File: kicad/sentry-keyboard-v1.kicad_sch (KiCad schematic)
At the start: 272 parts, among them J1 USB_C_Receptacle_USB2.0, J4 AVR-ISP-6, SW1 Reset, SW2 RotaryEncoder_Switch, U1 ATmega32U4-AU, U3 PRTR5V0U2X, Y1 16Mhz

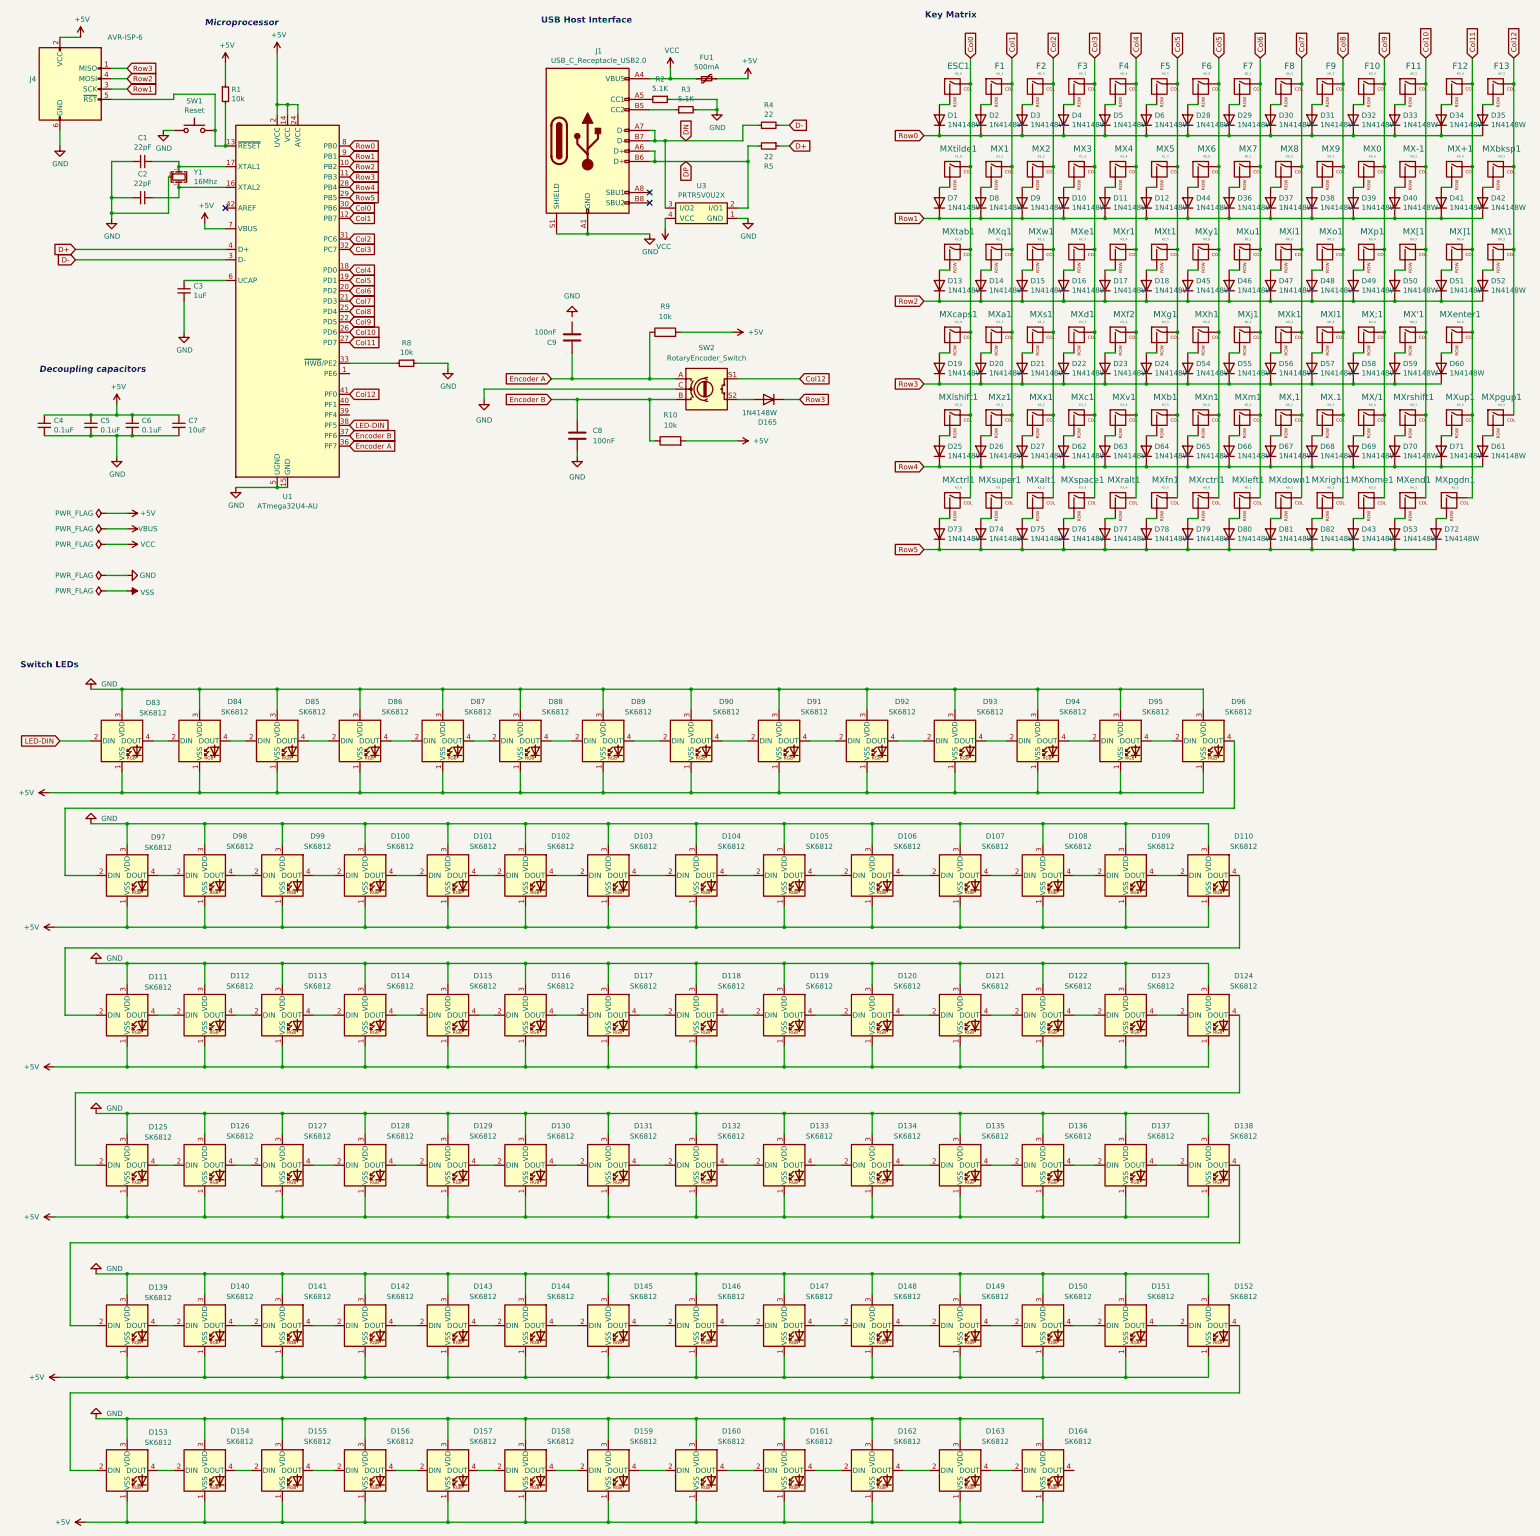
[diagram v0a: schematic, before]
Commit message: Get ERC to pass
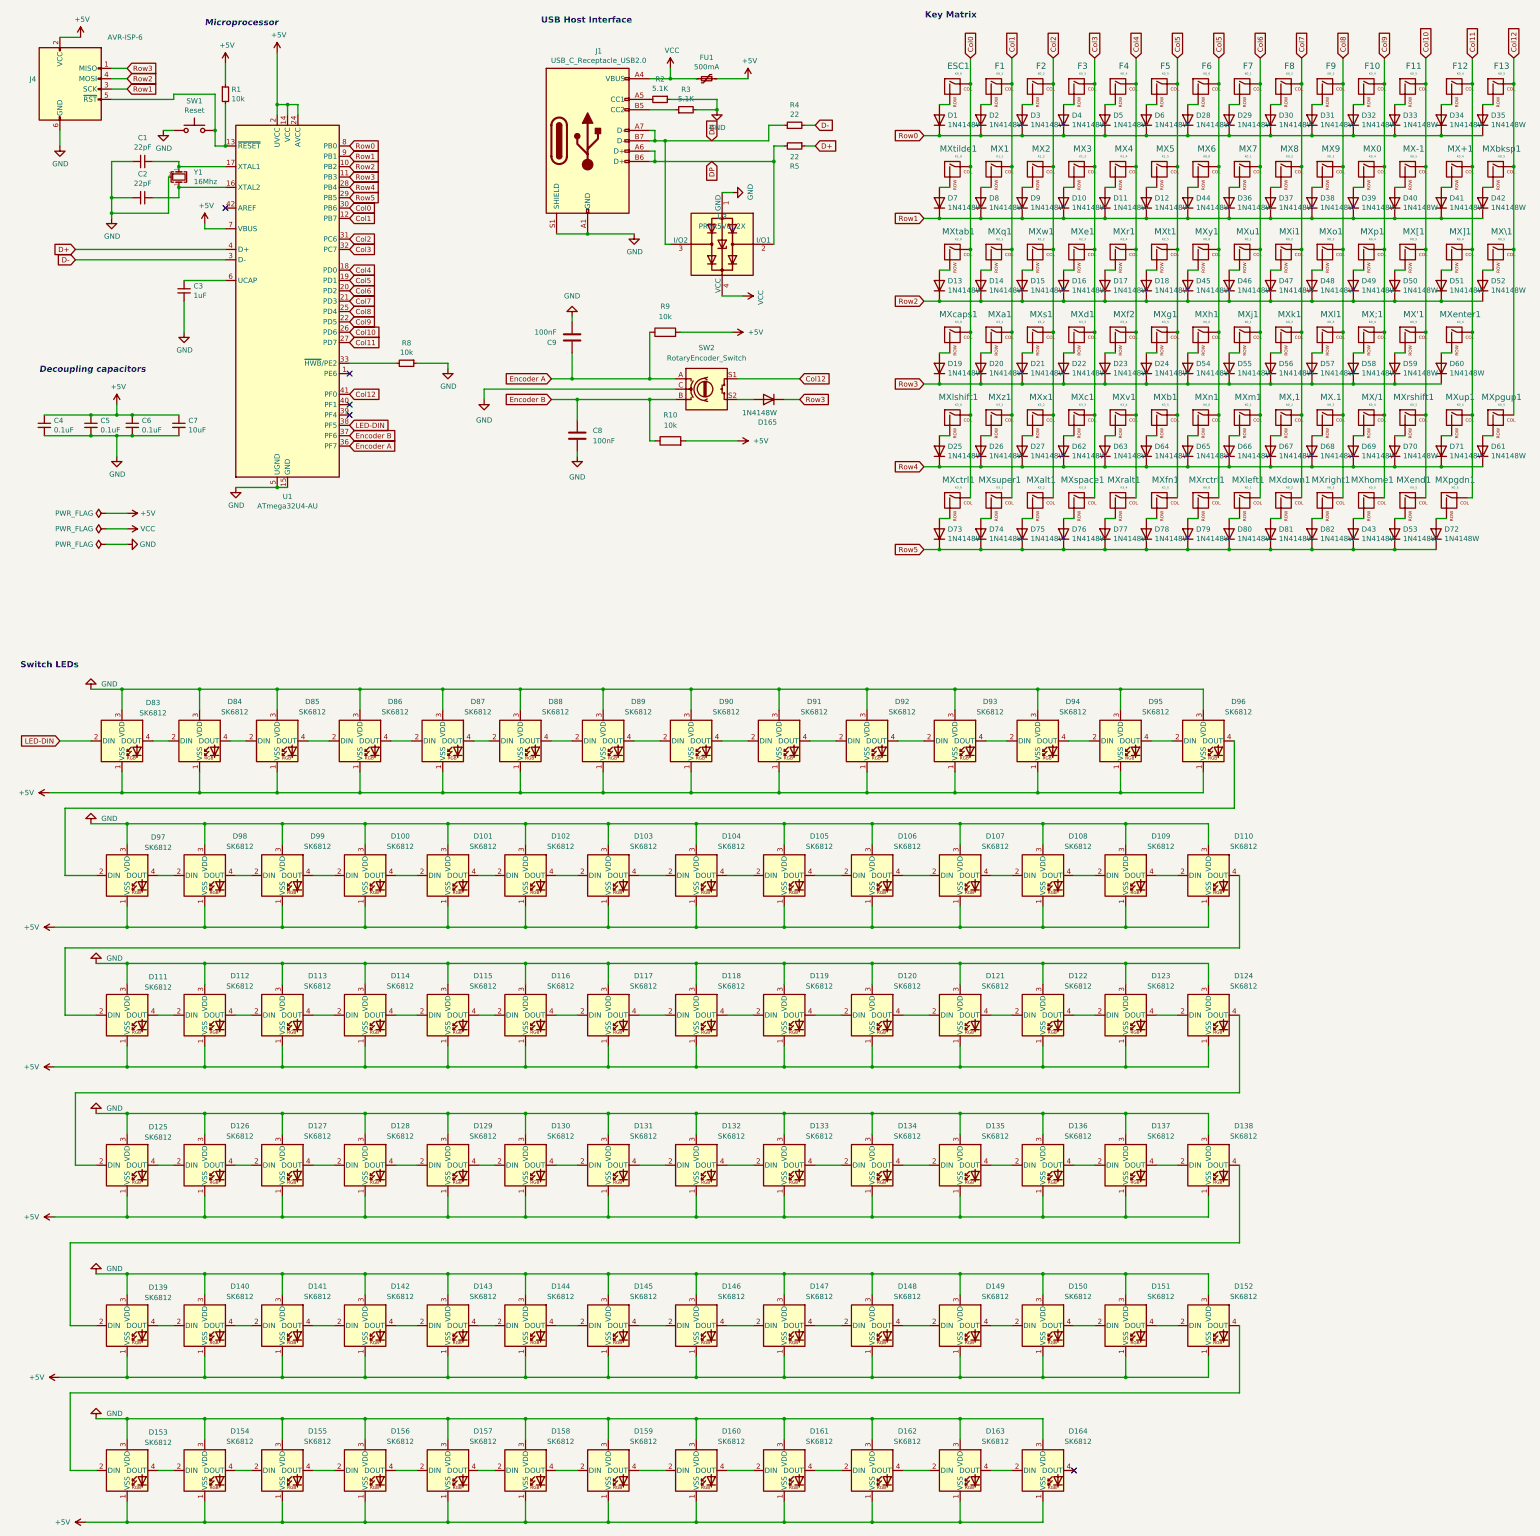
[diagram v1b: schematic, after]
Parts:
- J1: symbol Connector:USB_C_Receptacle_USB2.0 -> Connector:USB_C_Receptacle_USB2.0_14P
- U1: symbol MCU_Microchip_ATmega:ATmega32U4-AU -> MCU_Microchip_ATmega:ATmega32U4-A
- U3: footprint Keebio:SOT-143B -> Package_TO_SOT_SMD:SOT-143; symbol keebio:PRTR5V0U2X -> Power_Protection:PRTR5V0U2X
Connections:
- net GND: now also C9.2
- no-connect marks 3 -> 5
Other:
- moved on the sheet: R4, R5

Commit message: Place more footprints.
Now I have to do a lot of measuring and get all the keyswitch locations
dialed in.
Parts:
- MX\1: footprint Kaihl hotswap:MX-Hotswap-1U -> Kaihl hotswap:MX-Hotswap-1.25U
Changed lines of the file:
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@@
 	)
 	(symbol
+		(lib_name "MX-NoLED_1")
 		(lib_id "MX_Alps_Hybrid:MX-NoLED")
 		(at 378.46 76.2 0)
@@
 			)
 		)
-		(property "Footprint" "Kaihl hotswap:MX-Hotswap-1U"
+		(property "Footprint" "Kaihl hotswap:MX-Hotswap-1.25U"
 			(at 362.585 76.835 0)
 			(effects
@@
 					(size 1.27 1.27)
 				)
+				(hide yes)
 			)
 		)

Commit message: Place more footprints
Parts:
- F1: footprint Fuse:Fuse_1206_3216Metric_Pad1.42x1.75mm_HandSolder -> Kaihl hotswap:MX-Hotswap-1U
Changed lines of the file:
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@@
 			)
 		)
-		(property "Footprint" "Fuse:Fuse_1206_3216Metric_Pad1.42x1.75mm_HandSolder"
+		(property "Footprint" "Kaihl hotswap:MX-Hotswap-1U"
 			(at 239.395 36.195 0)
 			(effects

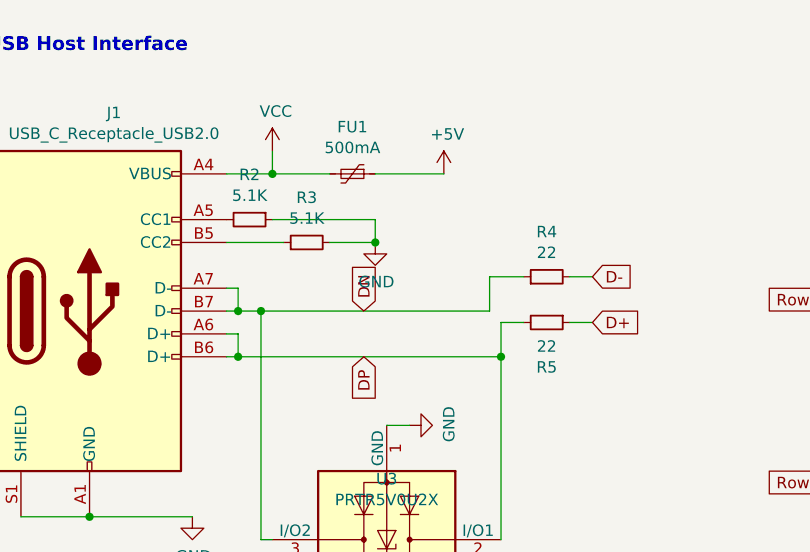
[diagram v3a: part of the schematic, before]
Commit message: All components roughly placed
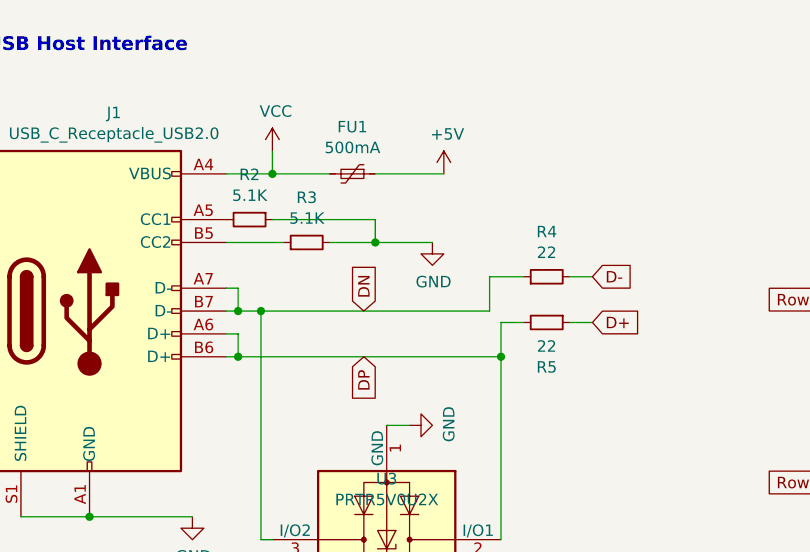
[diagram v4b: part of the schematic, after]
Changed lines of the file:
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@@
 	(wire
 		(pts
+			(xy 193.04 40.64) (xy 186.69 40.64)
+		)
+		(stroke
+			(width 0)
+			(type default)
+		)
+	)
+	(wire
+		(pts
 			(xy 158.75 208.28) (xy 180.34 208.28)
 		)
@@
 	(symbol
 		(lib_id "power:GND")
-		(at 186.69 40.64 0)
+		(at 193.04 40.64 0)
 		(unit 1)
 		(exclude_from_sim no)
@@
 		(dnp no)
 		(property "Reference" "#PWR0126"
-			(at 186.69 46.99 0)
+			(at 193.04 46.99 0)
 			(effects
 				(font
@@
 		)
 		(property "Value" "GND"
-			(at 186.817 45.0342 0)
+			(at 193.167 45.0342 0)
 			(effects
 				(font
@@
 		)
 		(property "Footprint" ""
-			(at 186.69 40.64 0)
+			(at 193.04 40.64 0)
 			(effects
 				(font
@@
 		)
 		(property "Datasheet" ""
-			(at 186.69 40.64 0)
+			(at 193.04 40.64 0)
 			(effects
 				(font
@@
 		)
 		(property "Description" ""
-			(at 186.69 40.64 0)
+			(at 193.04 40.64 0)
 			(effects
 				(font

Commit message: Dial in positions of a few keys and change the footprint of the usb connection.
I need to find out what the keyboard's daughter card has on it, as this
could be simpler to build.
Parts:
- J1: footprint Connector_JST:JST_GH_SM05B-GHS-TB_1x05-1MP_P1.25mm_Horizontal -> Keebio:USB_miniB_HandSolder
- MXrctrl1: footprint Kaihl hotswap:MX-Hotswap-1.25U -> Kaihl hotswap:MX-Hotswap-1U
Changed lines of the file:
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@@
 			)
 		)
-		(property "Footprint" "Connector_JST:JST_GH_SM05B-GHS-TB_1x05-1MP_P1.25mm_Horizontal"
+		(property "Footprint" "Keebio:USB_miniB_HandSolder"
 			(at 158.75 48.26 0)
 			(effects
@@
 			)
 		)
-		(property "Footprint" "Kaihl hotswap:MX-Hotswap-1.25U"
+		(property "Footprint" "Kaihl hotswap:MX-Hotswap-1U"
 			(at 290.195 137.795 0)
 			(effects

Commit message: More incremental progress.
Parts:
- MXralt1: footprint Kaihl hotswap:MX-Hotswap-1.25U -> Kaihl hotswap:MX-Hotswap-1U
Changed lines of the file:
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@@
 			)
 		)
-		(property "Footprint" "Kaihl hotswap:MX-Hotswap-1.25U"
+		(property "Footprint" "Kaihl hotswap:MX-Hotswap-1U"
 			(at 269.875 137.795 0)
 			(effects

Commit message: Get row 4 placed.
Had to change the size of several switches as they were wrong.
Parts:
- MXenter1: footprint Kaihl hotswap:MX-Hotswap-1.5U -> Kaihl hotswap:MX-Hotswap-2.25U
- MXlshift1: footprint Kaihl hotswap:MX-Hotswap-2U -> Kaihl hotswap:MX-Hotswap-2.25U
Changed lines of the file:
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@@
 			)
 		)
-		(property "Footprint" "Kaihl hotswap:MX-Hotswap-2U"
+		(property "Footprint" "Kaihl hotswap:MX-Hotswap-2.25U"
 			(at 229.235 117.475 0)
 			(effects
@@
 			)
 		)
-		(property "Footprint" "Kaihl hotswap:MX-Hotswap-1.5U"
+		(property "Footprint" "Kaihl hotswap:MX-Hotswap-2.25U"
 			(at 352.425 97.155 0)
 			(effects

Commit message: Place row 1
Fix \ footprint as it looks like 1.5u is the right size. I have to
remeasure to be sure.
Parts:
- MX\1: footprint Kaihl hotswap:MX-Hotswap-1.25U -> Kaihl hotswap:MX-Hotswap-1.5U
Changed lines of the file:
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@@
 			)
 		)
-		(property "Footprint" "Kaihl hotswap:MX-Hotswap-1.25U"
+		(property "Footprint" "Kaihl hotswap:MX-Hotswap-1.5U"
 			(at 362.585 76.835 0)
 			(effects
